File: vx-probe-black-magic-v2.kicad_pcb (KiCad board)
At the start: 2 copper layers, 72.4 x 41.9 mm, 44 parts, among them P1 USB MINI B, P10 CONN_01X01, P11 CONN_01X11, P12 CONN_01X03, P2 +5v power input, P3 +5v external input, P4 CONN_02X05, P5 CONN_01X04, P6 swdio/jtag, P7 CONN_01X01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

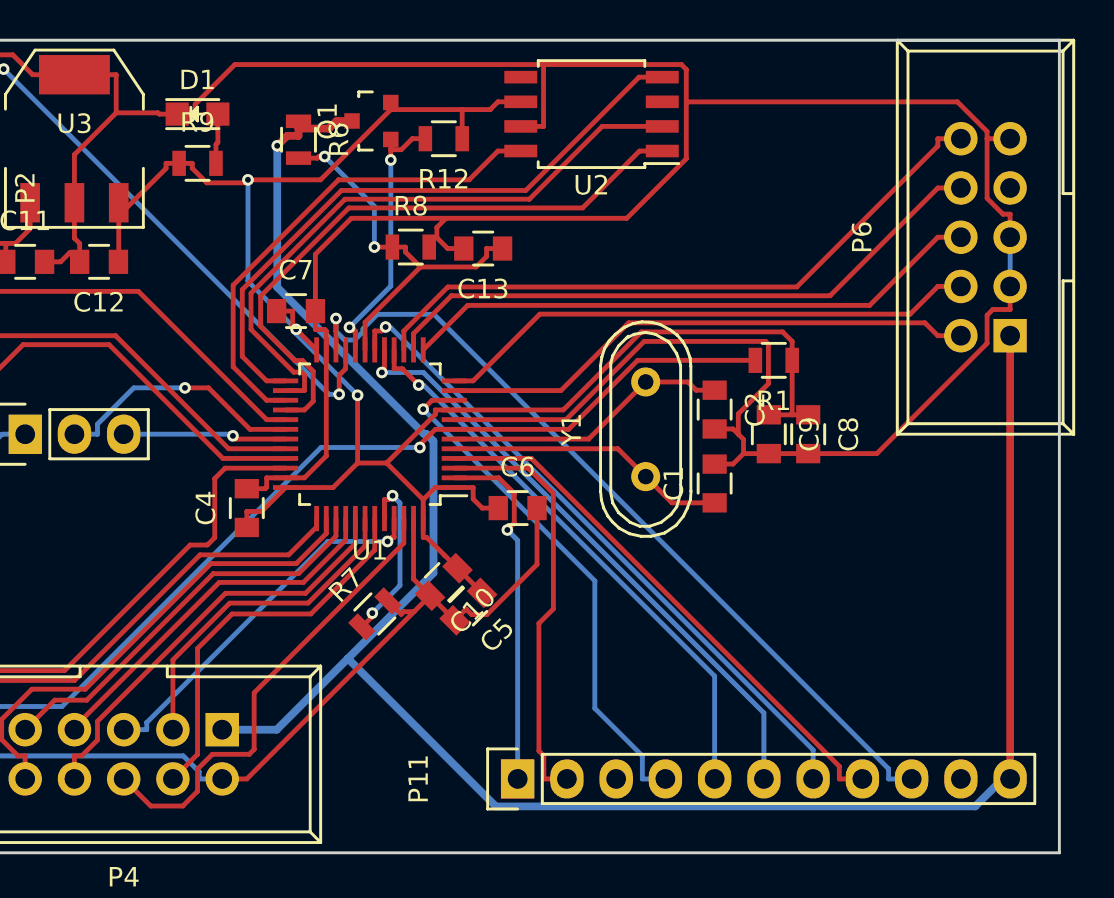
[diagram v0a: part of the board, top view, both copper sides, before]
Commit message: added a button
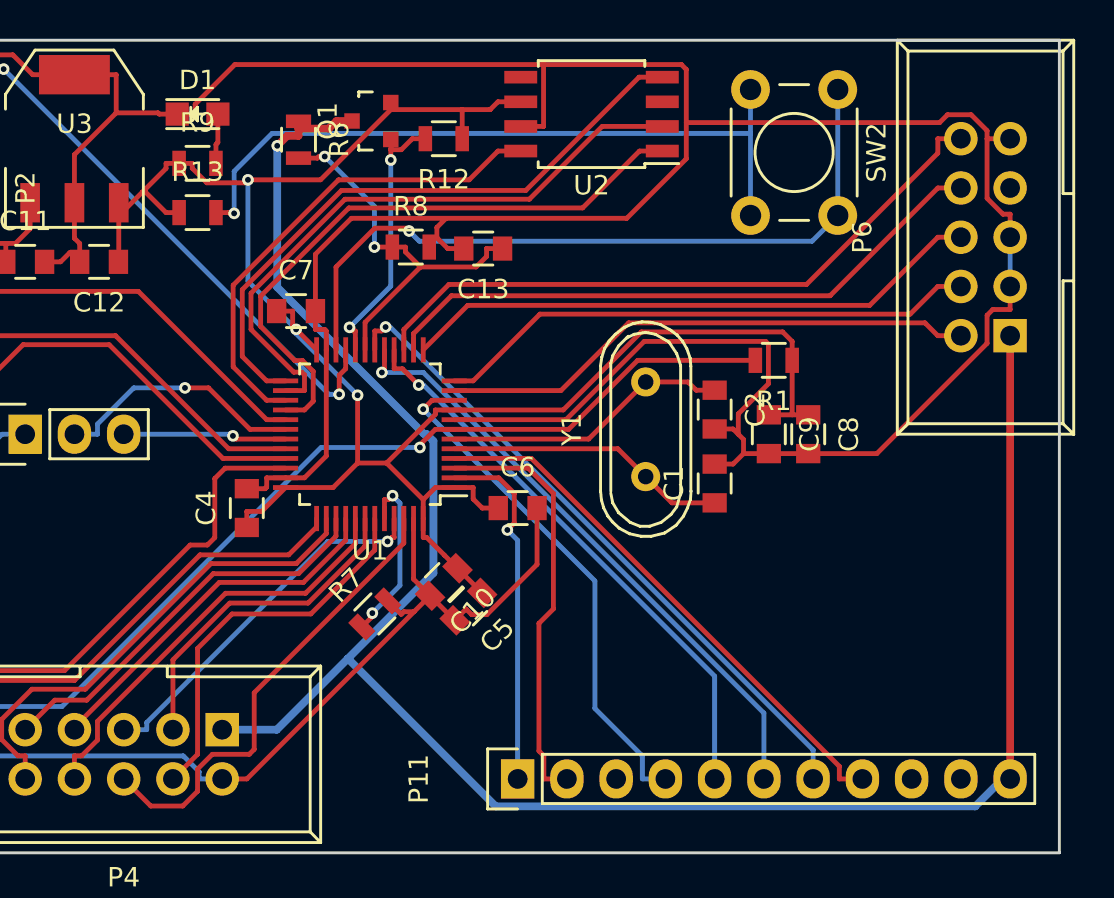
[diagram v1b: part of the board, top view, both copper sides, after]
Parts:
- added R13: 10k, Resistors_SMD:R_0805, F.Cu at (74.9, 48.3)
- added SW2: SW_PUSH, Buttons_Switches_ThroughHole:SW_PUSH_6mm, F.Cu at (108.0, 41.9)
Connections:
- P11 pad 9: /x8 -> Net-(P11-Pad9)
- U1 pad 22: /x8 -> /BTN1
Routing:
- net /x8: track 43.0 -> 0.00 mm, vias 1 -> 0
- net /BTN1: track 0.00 -> 38.3 mm, vias 0 -> 1
- net Net-(R13-Pad2): track 0.00 -> 37.1 mm, vias 0 -> 1
- net +3V3: track 102.2 -> 104.5 mm

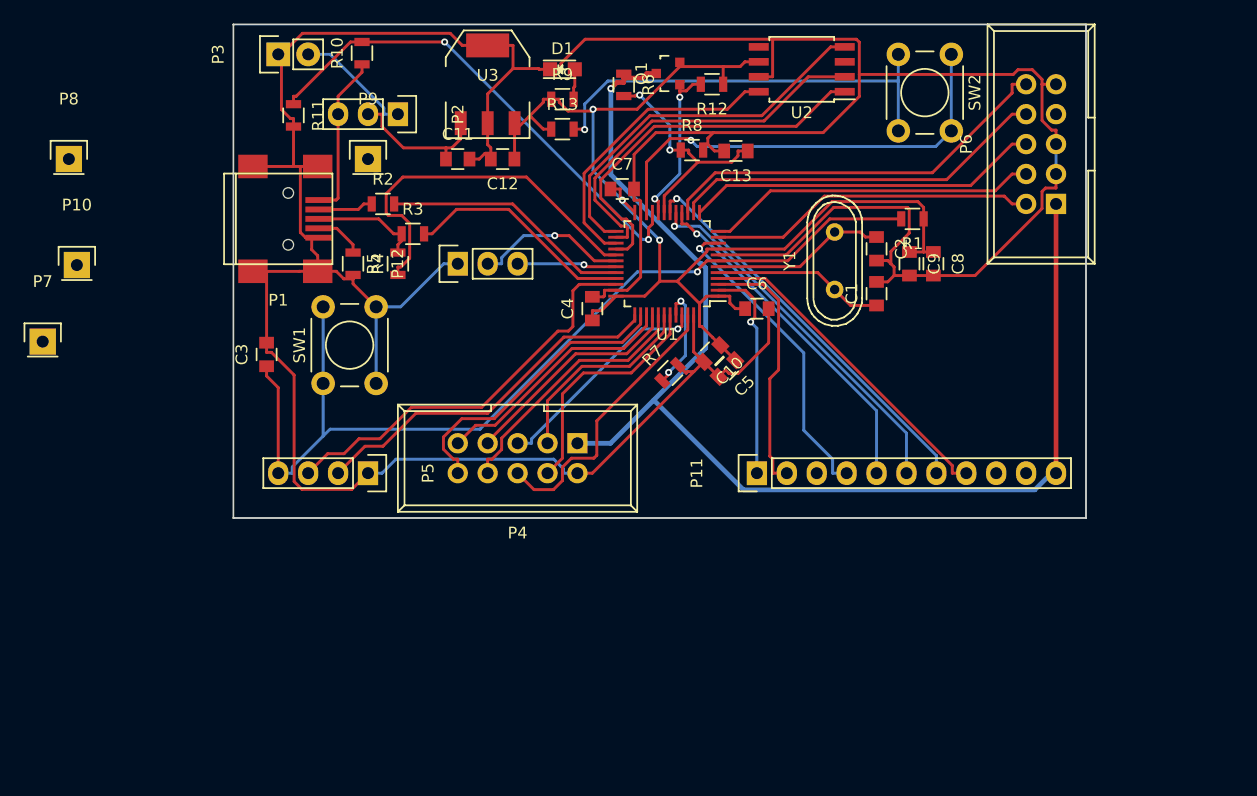
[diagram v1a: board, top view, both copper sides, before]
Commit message: added another button - this adds 4 vias!!!
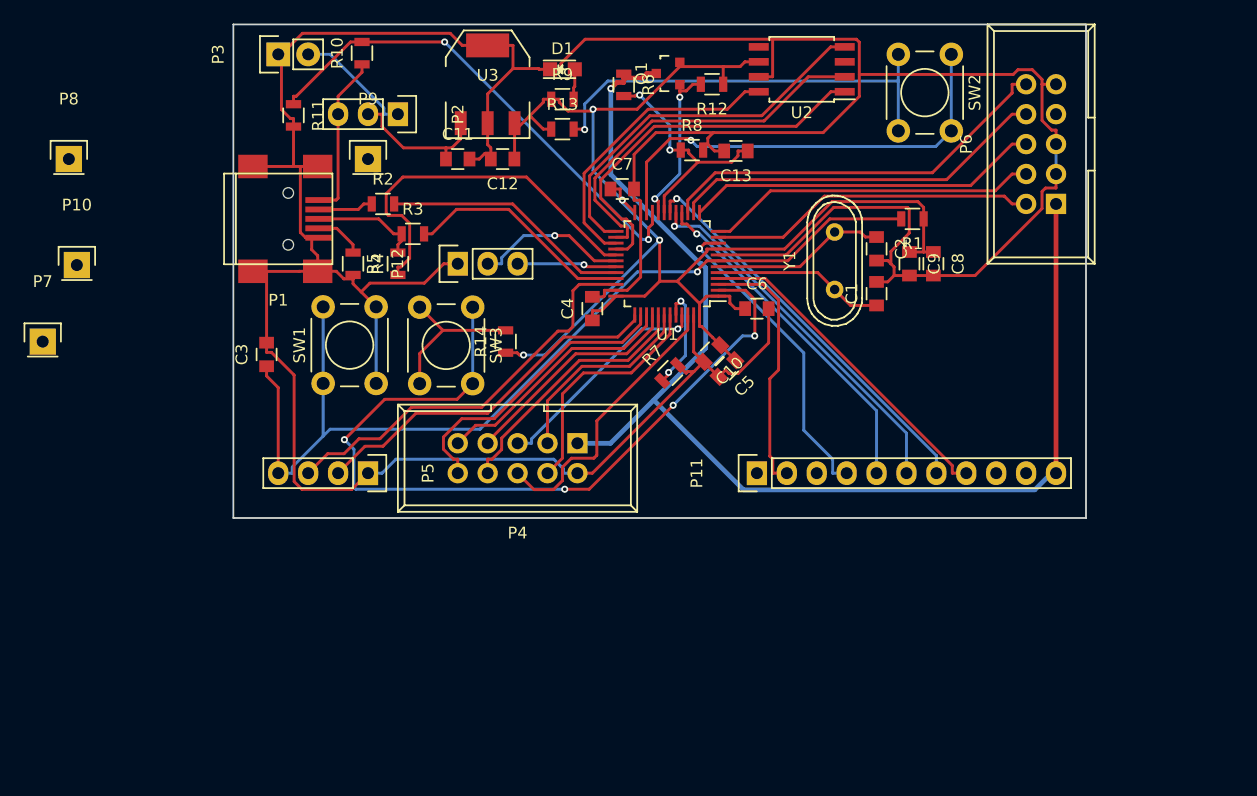
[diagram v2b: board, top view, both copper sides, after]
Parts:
- added R14: 10k, Resistors_SMD:R_0805, F.Cu at (70.1, 66.3)
- added SW3: SW_PUSH, Buttons_Switches_ThroughHole:SW_PUSH_6mm, F.Cu at (67.3, 63.4)
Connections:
- P11 pad 1: /x1 -> Net-(P11-Pad1)
- U1 pad 2: /x1 -> /BTN2
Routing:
- net /BTN2: track 0.00 -> 69.7 mm, vias 0 -> 4
- net /x1: track 18.5 -> 0.00 mm, vias 1 -> 0
- net +3V3: track 104.5 -> 121.8 mm, vias 3 -> 4
- net Net-(R14-Pad2): track 0.00 -> 13.5 mm
- net GND: track 317.1 -> 317.9 mm

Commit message: rerouted the extension connector
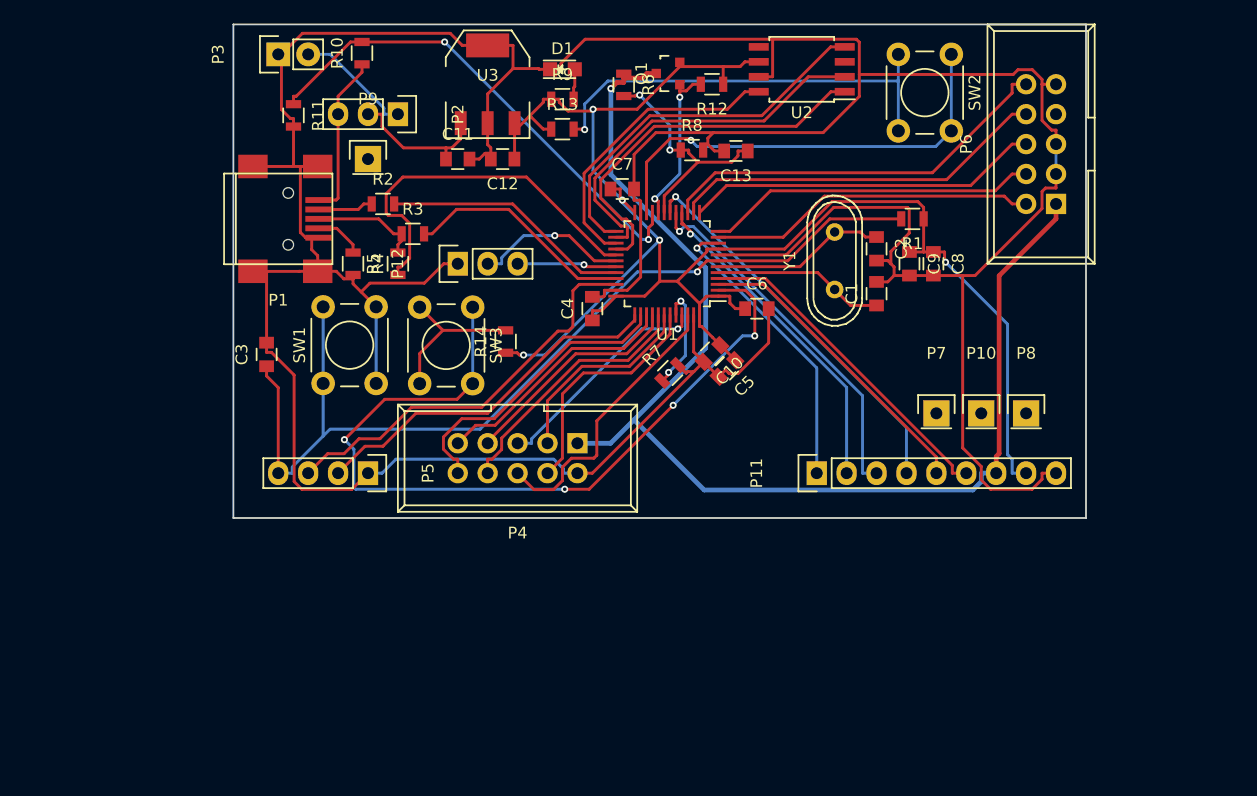
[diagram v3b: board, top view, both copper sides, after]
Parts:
- P11: value CONN_01X11 -> CONN_01X09; footprint Pin_Headers:Pin_Header_Straight_1x11 -> Pin_Headers:Pin_Header_Straight_1x09
- moved P8 84.1 mm to (114.3, 72.4)
- moved P10 77.8 mm to (110.5, 72.4)
- moved P7 76.1 mm to (106.7, 72.4)
- moved P11 5.08 mm to (96.5, 77.5)
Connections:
- P11 pad 1: Net-(P11-Pad1) -> /x4
- P11 pad 2: /x2 -> /x5
- P11 pad 3: Net-(P11-Pad3) -> /x6
- P11 pad 4: /x4 -> /x7
- P11 pad 5: /x5 -> /x2
- P11 pad 6: /x6 -> /x3
- P11 pad 7: /x7 -> /TPWR
- P11 pad 8: /x3 -> +3V3
- P11 pad 9: Net-(P11-Pad9) -> GND
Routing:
- net GND: track 317.9 -> 343.4 mm
- net +3V3: track 121.8 -> 145.0 mm, vias 4 -> 5
- net /x2: track 22.0 -> 26.0 mm
- net /TPWR: track 105.6 -> 103.9 mm
- net /x4: track 26.7 -> 25.3 mm
- net /x5: track 29.4 -> 28.1 mm
- net /x7: track 34.2 -> 33.2 mm

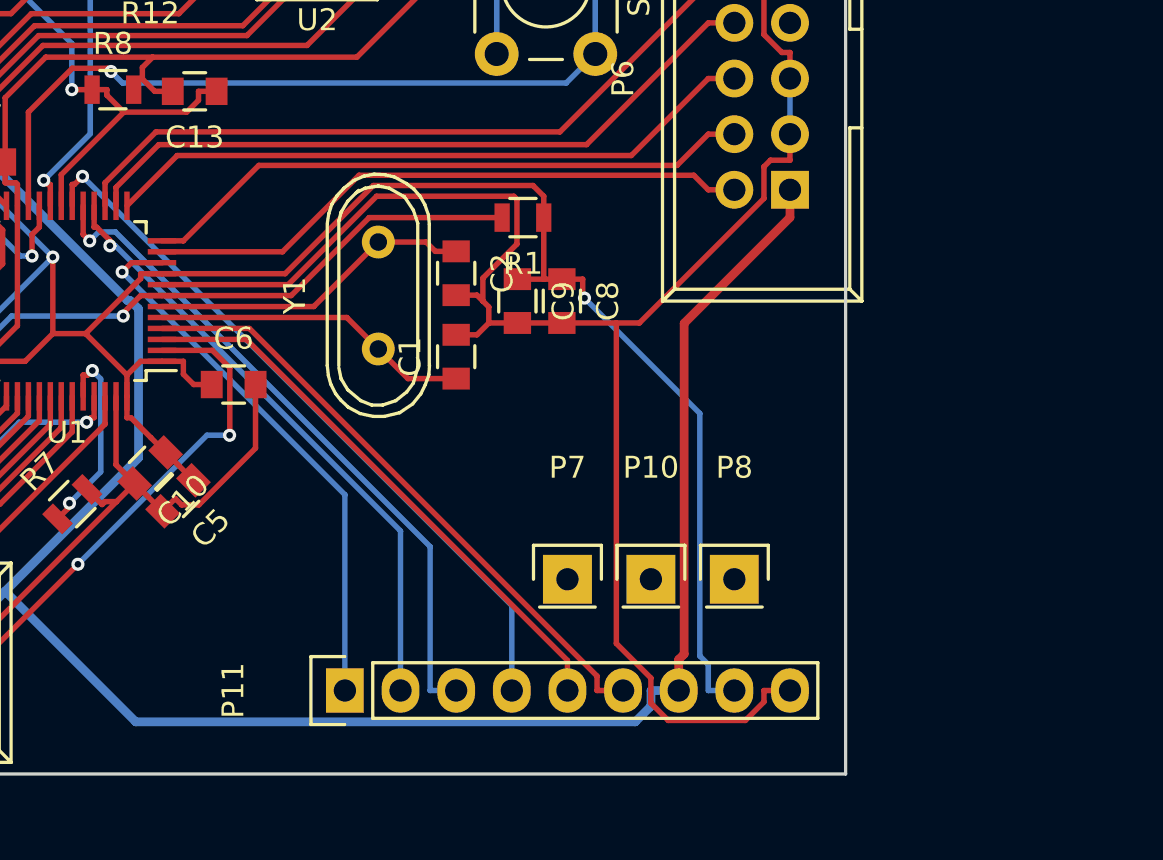
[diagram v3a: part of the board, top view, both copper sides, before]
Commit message: optimized extension connector routing
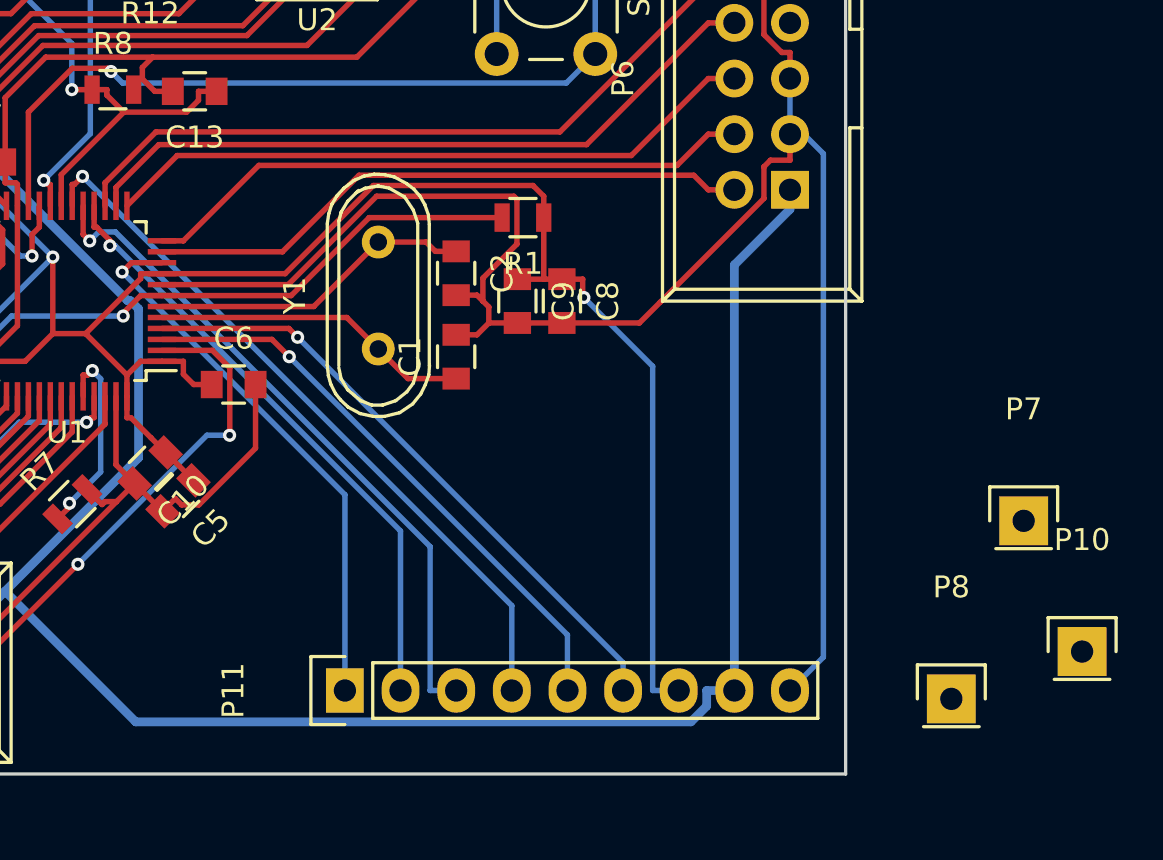
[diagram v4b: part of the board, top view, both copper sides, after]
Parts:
- moved P7 21.0 mm to (127.5, 69.7)
- moved P10 20.0 mm to (130.2, 75.7)
- moved P8 11.3 mm to (124.2, 77.9)
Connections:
- P11 pad 7: /TPWR -> +3V3
- P11 pad 8: +3V3 -> /TPWR
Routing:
- net /TPWR: track 103.9 -> 105.4 mm
- net GND: track 343.4 -> 344.9 mm
- net +3V3: track 145.0 -> 144.0 mm
- net /x2: track 26.0 -> 26.6 mm, vias 0 -> 1
- net /x3: track 28.3 -> 28.6 mm, vias 0 -> 1

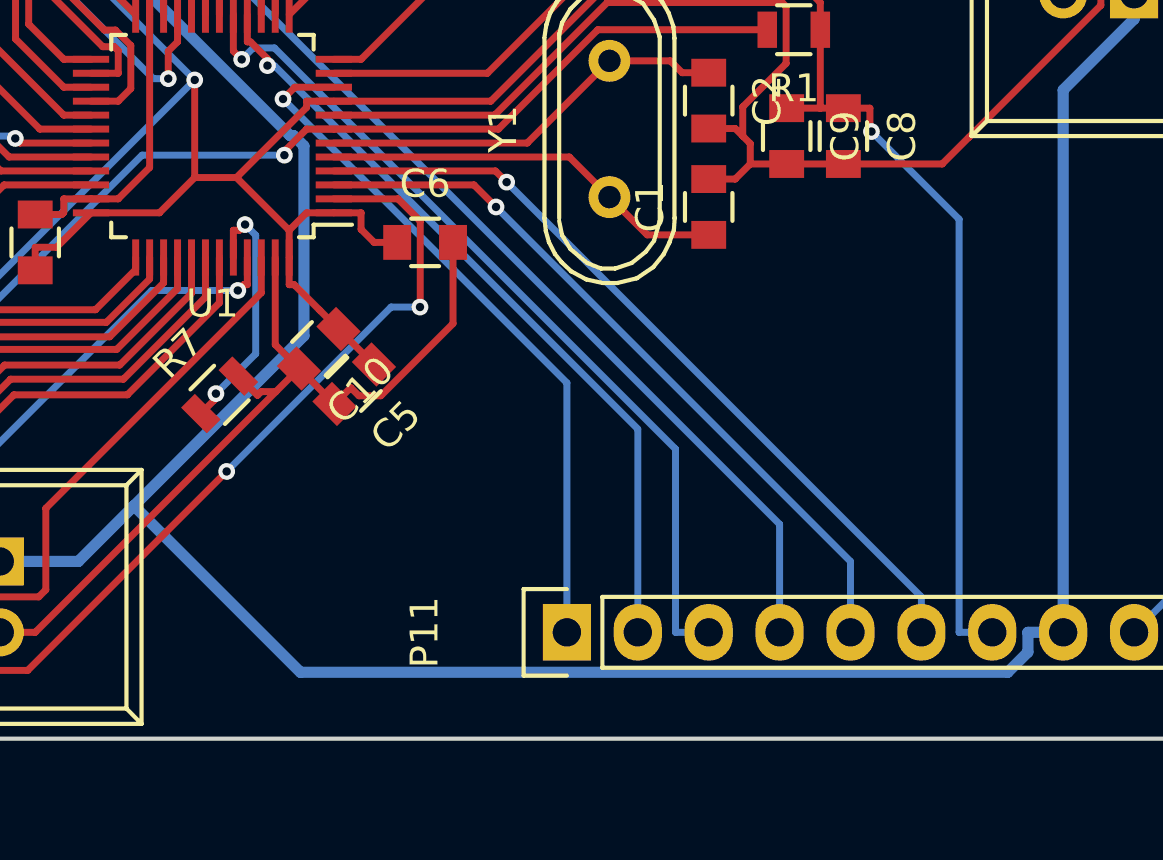
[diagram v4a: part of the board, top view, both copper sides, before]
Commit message: added two led-s
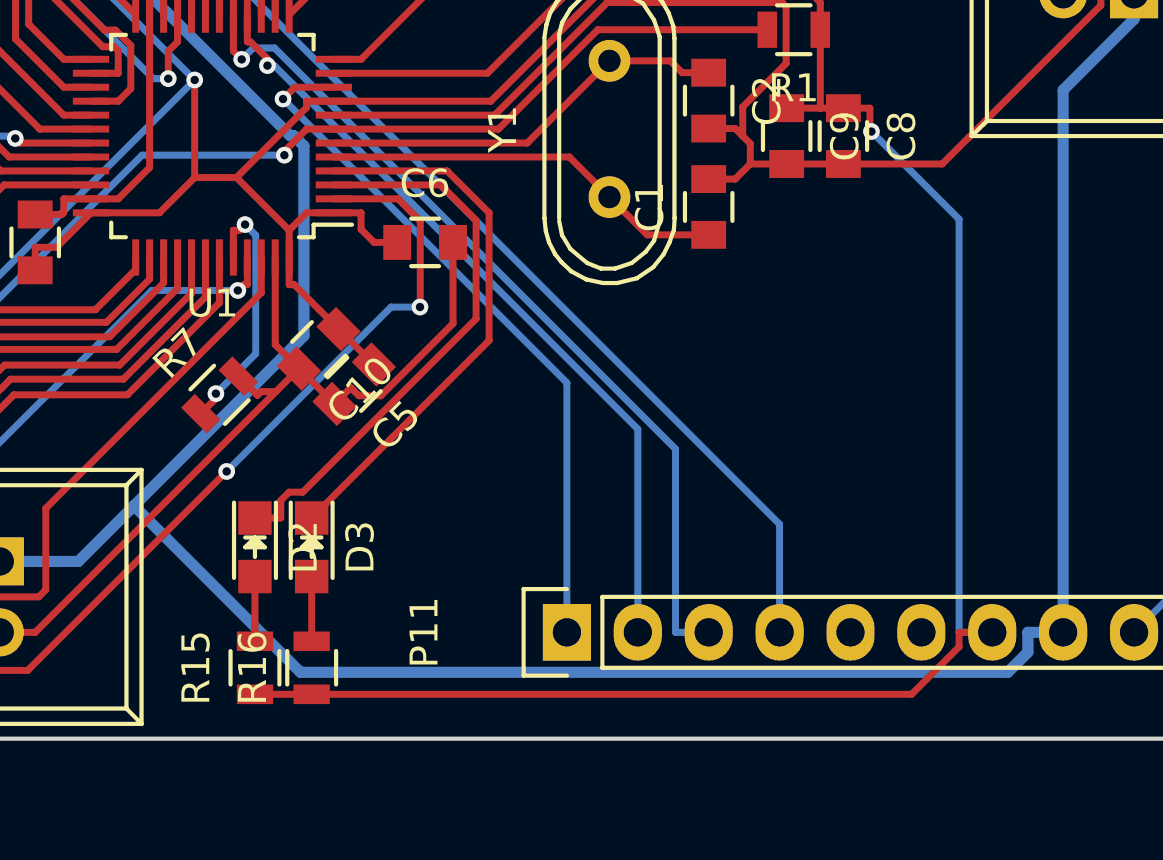
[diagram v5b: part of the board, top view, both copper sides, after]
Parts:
- added D2: Led_Small, LEDs:LED_0805, F.Cu at (85.3, 74.4)
- added D3: Led_Small, LEDs:LED_0805, F.Cu at (87.4, 74.4)
- added R15: 560R, Resistors_SMD:R_0805, F.Cu at (85.3, 78.7)
- added R16: 560R, Resistors_SMD:R_0805, F.Cu at (87.4, 78.7)
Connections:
- U1 pad 3: /x2 -> /LED1
- U1 pad 4: /x3 -> /LED2
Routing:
- net /x3: track 28.6 -> 0.00 mm, vias 1 -> 0
- net +3V3: track 144.0 -> 171.6 mm
- net /x2: track 26.6 -> 0.00 mm, vias 1 -> 0
- net /LED1: track 0.00 -> 20.4 mm
- net /LED2: track 0.00 -> 19.7 mm
- net Net-(D3-Pad2): track 0.00 -> 2.32 mm
- net Net-(D2-Pad2): track 0.00 -> 2.32 mm
